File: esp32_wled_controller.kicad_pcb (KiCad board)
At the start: 4 copper layers, 95 x 95 mm, 83 parts, among them J1 USB_C_Receptacle_USB2.0_16P, J2 Screw_Terminal_01x03, J3 Screw_Terminal_01x03, J4 Screw_Terminal_01x03, J5 Screw_Terminal_01x03, J6 Screw_Terminal_01x02, J7 Screw_Terminal_01x02, K1 SRD-05VDC-SL-C, K2 SRD-05VDC-SL-C, K3 SRD-05VDC-SL-C, K4 SRD-05VDC-SL-C, Q1 Q_NPN_BEC, Q2 Q_NPN_BEC, Q3 BC547A, Q4 BC547A, Q5 BC547A, Q6 BC547A, U1 USBLC6-2P6, U2 AMS1117-3.3, U3 CP2104, U4 ESP32-SOLO1, U5 PC817, U6 PC817, U7 PC817, U8 PC817, U9 SN74AHCT125PWR

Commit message: board revision 1.1
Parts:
- removed H1, H2, H3, H4: MountingHole, MountingHole:MountingHole_2.7mm_M2.5_DIN965_Pad
- removed RX1, TX1: TestPoint, TestPoint:TestPoint_Pad_D1.0mm
- removed U4: ESP32-SOLO1, lib:ESP32SOLO1
- added H5: MountingHole_Pad, MountingHole:MountingHole_2.5mm_Pad, F.Cu at (112.1, 25.3)
- added H6: MountingHole_Pad, MountingHole:MountingHole_2.5mm_Pad, F.Cu at (25.9, 25.1)
- added H7: MountingHole_Pad, MountingHole:MountingHole_2.5mm_Pad, F.Cu at (25.4, 111.9)
- added H8: MountingHole_Pad, MountingHole:MountingHole_2.5mm_Pad, F.Cu at (112.1, 111.9)
- added RX2: TestPoint, TestPoint:TestPoint_Pad_D1.0mm, F.Cu at (88.6, 43.5)
- added TX2: TestPoint, TestPoint:TestPoint_Pad_D1.0mm, F.Cu at (85.3, 43.6)
- added U10: ESP32-S2-WROOM, lib:XCVR_ESP32-S2-WROOM, F.Cu at (107.0, 46.3)
- Q1, Q2: value Q_NPN_BEC -> SS8050
- moved 3.3V1 24.6 mm to (78.6, 43.5)
- moved GND1 23.5 mm to (81.9, 43.5)
- moved Q5 13.0 mm to (79.9, 69.0)
- moved R23 13.0 mm to (92.3, 96.1)
- moved RELAY3 13.0 mm to (75.9, 64.8)
- moved Q3 13.0 mm to (35.6, 68.8)
- moved C10 13.0 mm to (64.8, 39.3)
- moved C11 13.0 mm to (65.5, 37.4)
- moved C2 13.0 mm to (102.4, 32.5)
- moved C4 13.0 mm to (66.5, 55.5)
- moved C9 13.0 mm to (66.1, 46.1)
- moved R1 13.0 mm to (79.2, 33.3)
- moved R10 13.0 mm to (75.4, 36.3)
- moved R11 13.0 mm to (75.4, 37.5)
- moved R13 13.0 mm to (56.9, 59.5)
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- renumbered SW-BOOT1 to BOOT, SW-RESET1 to RESET
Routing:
- net /IO0: track 66.4 -> 44.5 mm
- net /STRIP4: track 47.6 -> 26.9 mm
- net /STRIP3: track 41.2 -> 24.3 mm
- net /EN: track 49.5 -> 65.3 mm
- net /IO17_RELAYS: track 93.5 -> 109.2 mm
- net /STRIP2: track 39.4 -> 26.8 mm
- net /STRIP1: track 40.3 -> 29.4 mm
- net /RX: track 47.5 -> 53.9 mm
- net GND: track 273.8 -> 270.2 mm, vias 6 -> 7
- net +3.3V: track 123.5 -> 120.9 mm
- net /TX: track 48.1 -> 45.8 mm
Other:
- board text removed: "ESP32"

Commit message: board rev 1.2, cleanup
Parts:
- removed 3.3V1, RX2, TX2: TestPoint, TestPoint:TestPoint_Pad_D1.0mm
- removed BOOT, RESET: SW_SPST, lib:TS-1187A-B-A-B
- removed C14: 100nF, Capacitor_SMD:C_0402_1005Metric_Pad0.74x0.62mm_HandSolder
- removed D5, D6, D7: 1N4007, Diode_SMD:D_MELF_Handsoldering
- removed H5: MountingHole_Pad, MountingHole:MountingHole_2.5mm_Pad
- removed R12: 1K, Resistor_SMD:R_0402_1005Metric_Pad0.72x0.64mm_HandSolder
- removed U10: ESP32-S2-WROOM, lib:XCVR_ESP32-S2-WROOM
- added 3V3: TestPoint, TestPoint:TestPoint_Pad_D1.5mm, F.Cu at (84.2, 30.3)
- added D1: C7420350, Diode_SMD:D_MELF_Handsoldering, F.Cu at (82.7, 73.2)
- added D2: C7420350, Diode_SMD:D_MELF_Handsoldering, F.Cu at (60.4, 73.1)
- added D3: C7420350, Diode_SMD:D_MELF_Handsoldering, F.Cu at (38.3, 73.1)
- added RE1: SolderJumper_2_Bridged, Jumper:SolderJumper-2_P1.3mm_Open_TrianglePad1.0x1.5mm, F.Cu at (77.5, 50.4)
- added RE2: SolderJumper_2_Bridged, Jumper:SolderJumper-2_P1.3mm_Open_TrianglePad1.0x1.5mm, F.Cu at (82.0, 50.4)
- added RE3: SolderJumper_2_Bridged, Jumper:SolderJumper-2_P1.3mm_Open_TrianglePad1.0x1.5mm, F.Cu at (86.4, 50.4)
- added REF**: OSHW-Logo_11.4x12mm_SilkScreen, Symbol:OSHW-Logo_11.4x12mm_SilkScreen, B.Cu at (108.1, 34.4)
- added RX1: TestPoint, TestPoint:TestPoint_Pad_D1.5mm, F.Cu at (114.1, 44.0)
- added SW-BOOT1: SW_SPST, lib:TS-1187A-B-A-B, F.Cu at (85.9, 36.7)
- added SW-RESET1: SW_SPST, lib:TS-1187A-B-A-B, F.Cu at (85.9, 43.5)
- added TX1: TestPoint, TestPoint:TestPoint_Pad_D1.5mm, F.Cu at (114.0, 39.5)
- added U4: EL817, Package_DIP:DIP-4_W7.62mm, F.Cu at (79.4, 61.4)
- D9: value 1N4007 -> C7420350
- GND1: footprint TestPoint:TestPoint_Pad_D1.0mm -> TestPoint:TestPoint_Pad_D1.5mm
- Q3, Q4, Q5, Q6: value BC547A -> SS8050; footprint Package_TO_SOT_SMD:TSOT-23_HandSoldering -> Package_TO_SOT_SMD:SOT-23
- U5, U6, U7: value PC817 -> EL817; footprint Package_DIP:SMDIP-4_W7.62mm -> Package_DIP:DIP-4_W7.62mm
- U8: value PC817 -> ESP32-S2-WROOM-1-N4(4MB); footprint Package_DIP:SMDIP-4_W7.62mm -> lib:WIFI-SMD_ESP32-S2-WROVER-I
- moved U5 63.6 mm to (101.7, 61.3)
- moved U7 47.7 mm to (35.0, 61.4)
- moved C13 36.4 mm to (79.1, 42.4), turned to -90 degrees
- moved C12 34.6 mm to (78.6, 46.7)
- moved U9 26.2 mm to (69.0, 84.5)
- moved U8 23.8 mm to (101.7, 40.2)
- moved C4 23.4 mm to (67.7, 78.9)
- moved R7 15.7 mm to (90.5, 35.2), turned to 90 degrees
- moved R14 15.5 mm to (74.0, 73.9)
- moved R8 15.4 mm to (29.6, 73.8)
- moved R13 15.2 mm to (51.7, 73.8)
- moved R18 15.1 mm to (96.3, 73.8)
- moved GND1 14.5 mm to (87.9, 30.3), turned to 0 degrees
- moved C2 13.2 mm to (90.5, 38.2), turned to -90 degrees
- moved C1 13.1 mm to (90.5, 45.0), turned to 90 degrees
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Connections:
- C12 pad 1: /EN -> +3.3V
- C4 pad 1: Net-(U9-GND) -> GND
- C4 pad 2: Net-(U9-VCC) -> +5V
- K1 pad A2: Net-(D5-A) -> Net-(D3-A)
- K2 pad A2: Net-(D6-A) -> Net-(D2-A)
- K3 pad A2: Net-(D7-A) -> Net-(D1-A)
- Q3 pad 1: Net-(D5-A) -> Net-(Q3-B)
- Q3 pad 2: Net-(Q3-B) -> GND
- Q3 pad 3: GND -> Net-(D3-A)
- Q4 pad 1: Net-(D6-A) -> Net-(Q4-B)
- Q4 pad 2: Net-(Q4-B) -> GND
- Q4 pad 3: GND -> Net-(D2-A)
- Q5 pad 1: Net-(D7-A) -> Net-(Q5-B)
- Q5 pad 2: Net-(Q5-B) -> GND
- Q5 pad 3: GND -> Net-(D1-A)
- Q6 pad 1: Net-(D9-A) -> Net-(Q6-B)
- Q6 pad 2: Net-(Q6-B) -> GND
- Q6 pad 3: GND -> Net-(D9-A)
- RELAY1 pad 1: /IO17_RELAYS -> /RELAY1
- RELAY2 pad 1: /IO17_RELAYS -> /RELAY2
- RELAY3 pad 1: /IO17_RELAYS -> /RELAY3
- RELAY4 pad 1: /IO17_RELAYS -> /RELAY4
- U5 pad 1: Net-(R8-Pad1) -> Net-(R18-Pad1)
- U5 pad 2: Net-(RELAY1-A) -> Net-(RELAY4-A)
- U5 pad 3: Net-(R15-Pad1) -> Net-(R19-Pad1)
- U7 pad 1: Net-(R14-Pad1) -> Net-(R8-Pad1)
- U7 pad 2: Net-(RELAY3-A) -> Net-(RELAY1-A)
- U7 pad 3: Net-(R17-Pad1) -> Net-(R15-Pad1)
- U8 pad 1: Net-(R18-Pad1) -> GND
- U8 pad 2: Net-(RELAY4-A) -> +3.3V
- U8 pad 3: Net-(R19-Pad1) -> /IO0
- U8 pad 4: +5V -> unconnected-(U8-IO1-Pad4)
- U9 pad 1: Net-(U9-GND) -> GND
- U9 pad 10: Net-(U9-GND) -> GND
- U9 pad 13: Net-(U9-GND) -> GND
- U9 pad 14: Net-(U9-VCC) -> +5V
- U9 pad 4: Net-(U9-GND) -> GND
- U9 pad 7: Net-(U9-GND) -> GND
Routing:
- net GND: track 270.2 -> 114.3 mm, vias 7 -> 9
- net /IO17_RELAYS: track 109.2 -> 0.00 mm, vias 6 -> 0
- net /RELAY1: track 0.00 -> 78.0 mm, vias 0 -> 3
- net /RELAY2: track 0.00 -> 65.1 mm, vias 0 -> 3
- net /RELAY4: track 0.00 -> 54.4 mm, vias 0 -> 3
- net /STRIP2: track 26.8 -> 70.9 mm, vias 0 -> 2
- net /RELAY3: track 0.00 -> 41.0 mm, vias 0 -> 3
- net +3.3V: track 120.9 -> 81.5 mm, vias 5 -> 6
- net /STRIP1: track 29.4 -> 66.2 mm, vias 0 -> 2
- net +5V: track 188.6 -> 153.1 mm
- net /STRIP3: track 24.3 -> 59.0 mm
- net /STRIP4: track 26.9 -> 57.6 mm
- net Net-(U9-3Y): track 53.1 -> 25.5 mm
- net Net-(U9-4Y): track 57.0 -> 29.9 mm, vias 2 -> 0
- net Net-(U9-GND): track 26.4 -> 0.00 mm, vias 3 -> 0
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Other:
- board text added: "GND 5V"
- board text added: "KEEP-OUT ZONE"
- board text added: "PWR"
- board text added: "website: jack0217.dev github: @fellettigiacomo license: CERN-OHL-S"
- board text removed: "+5V GND"
- board text removed: "3.3V PWR"
- board text removed: "USB-C"

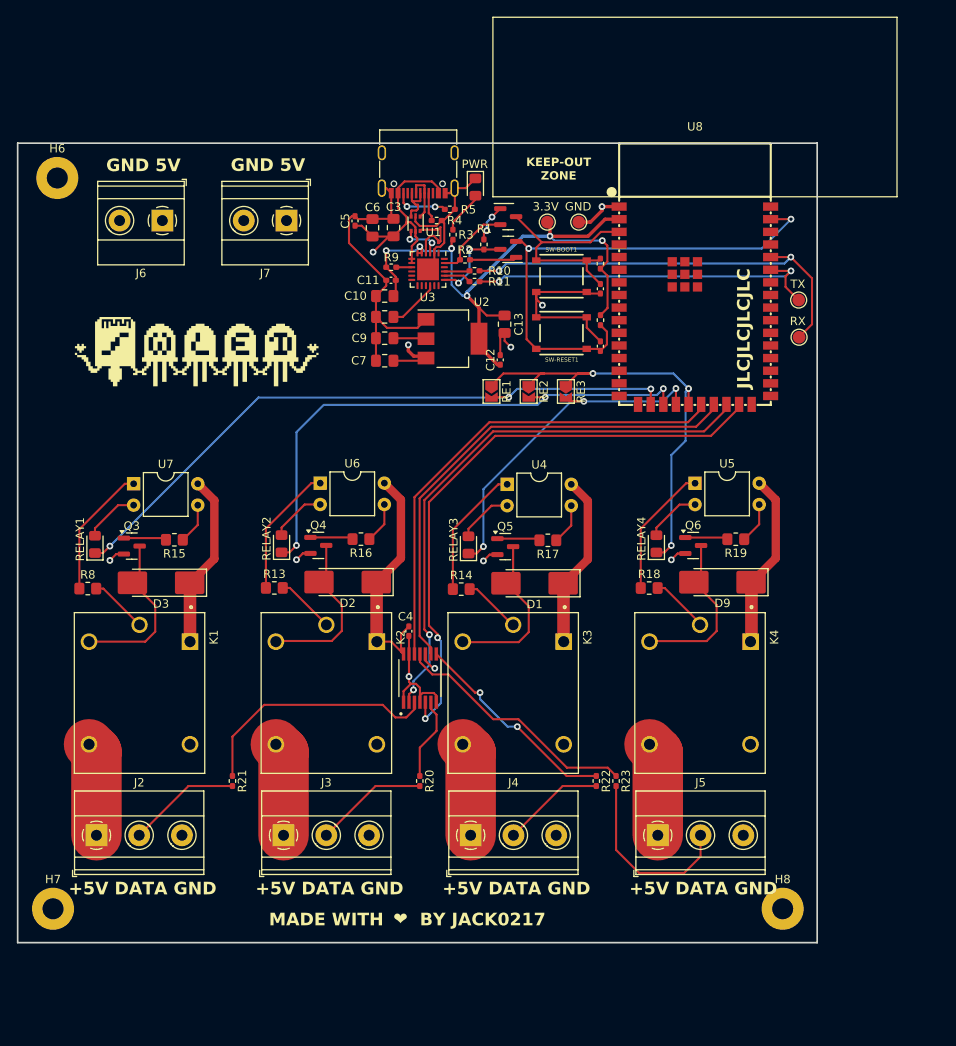
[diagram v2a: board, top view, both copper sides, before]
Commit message: changed terminal block footprint
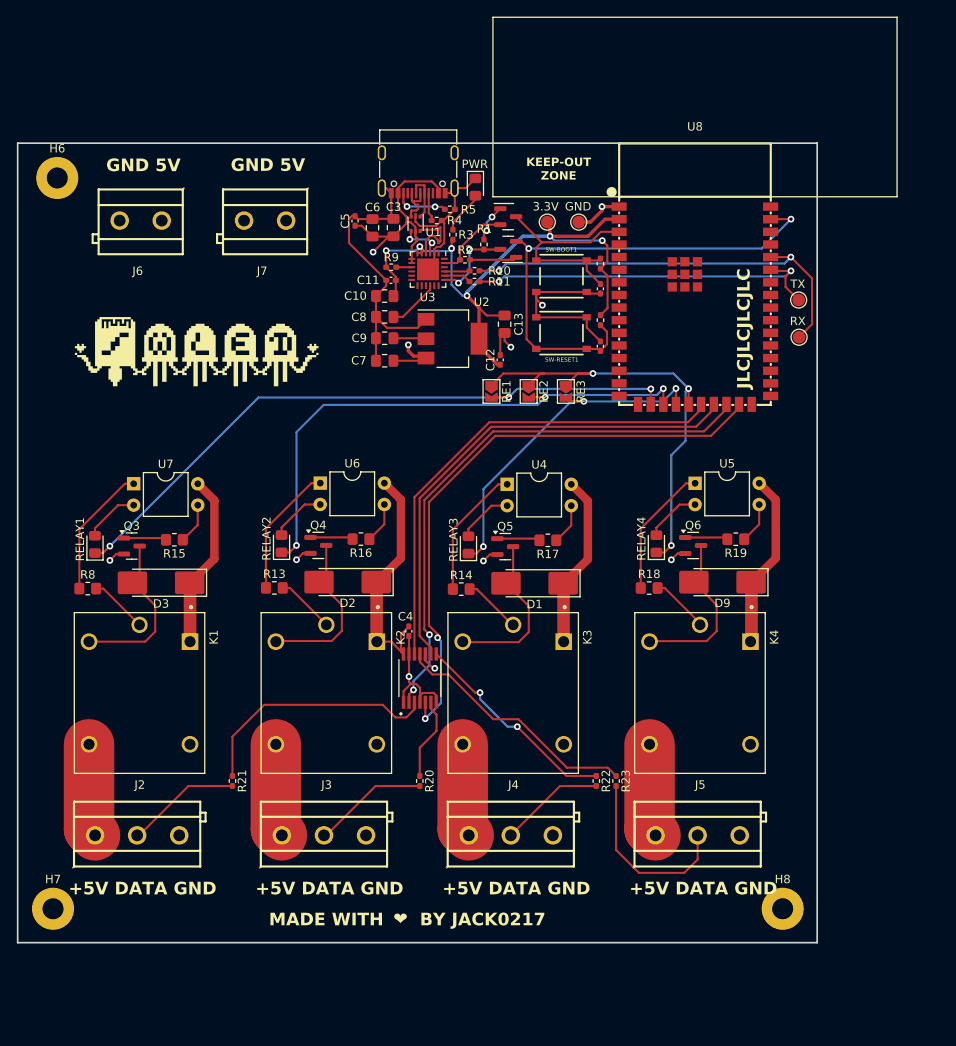
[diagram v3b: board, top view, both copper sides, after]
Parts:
- J2, J3, J4, J5: footprint TerminalBlock_Phoenix:TerminalBlock_Phoenix_MKDS-1,5-3-5.08_1x03_P5.08mm_Horizontal -> lib:CONN-TH_3P-P5.00_KF301-5.0-3P
- J6, J7: footprint TerminalBlock_Phoenix:TerminalBlock_Phoenix_MKDS-1,5-2-5.08_1x02_P5.08mm_Horizontal -> lib:CONN-TH_P5.00_KF301-5.0-2P
- moved J2 4.84 mm to (35.4, 103.2)
- moved J3 4.80 mm to (57.6, 103.2)
- moved J4 4.77 mm to (79.8, 103.2)
- moved J5 4.74 mm to (102.0, 103.2)
- moved J6 2.57 mm to (35.9, 30.1)
- moved J7 2.55 mm to (50.6, 30.1)

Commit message: final 1.2 release
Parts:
- removed SW-BOOT1, SW-RESET1: SW_SPST, lib:TS-1187A-B-A-B
- removed U1: USBLC6-2P6, Package_TO_SOT_SMD:SOT-666
- added SW1: SW_SPST, Button_Switch_SMD:SW_Push_1P1T_XKB_TS-1187A, F.Cu at (85.9, 43.4)
- added SW2: SW_SPST, Button_Switch_SMD:SW_Push_1P1T_XKB_TS-1187A, F.Cu at (85.9, 36.7)
- renumbered G*** to G***1, REF** to REF**1
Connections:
- J1 pad A6: Net-(J1-D+-PadA6) -> /D+
- J1 pad A7: Net-(J1-D--PadA7) -> /D-
- J1 pad B6: Net-(J1-D+-PadA6) -> /D+
- J1 pad B7: Net-(J1-D--PadA7) -> /D-
- J1 pad S1: GND -> unconnected-(J1-SHIELD-PadS1)_2
- U3 pad 3: Net-(U3-D+) -> /D+
- U3 pad 4: Net-(U3-D-) -> /D-
- U8 pad 42: unconnected-(U8-GND-Pad42) -> GND
- U8 pad 43: unconnected-(U8-GND-Pad43)_1 -> GND
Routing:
- net /D+: track 0.00 -> 13.6 mm, vias 0 -> 2
- net /D-: track 0.00 -> 12.0 mm, vias 0 -> 2
- net Net-(U3-D-): track 8.43 -> 0.00 mm
- net +3.3V: track 81.5 -> 87.8 mm
- net Net-(J1-D+-PadA6): track 5.86 -> 0.00 mm
- net Net-(J1-D--PadA7): track 5.86 -> 0.00 mm
- net Net-(U3-D+): track 5.07 -> 0.00 mm, vias 2 -> 0
- net +5V: track 153.1 -> 151.1 mm
- net GND: track 114.3 -> 113.8 mm, vias 9 -> 16
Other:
- board text added: "BOOT"
- board text added: "RESET"

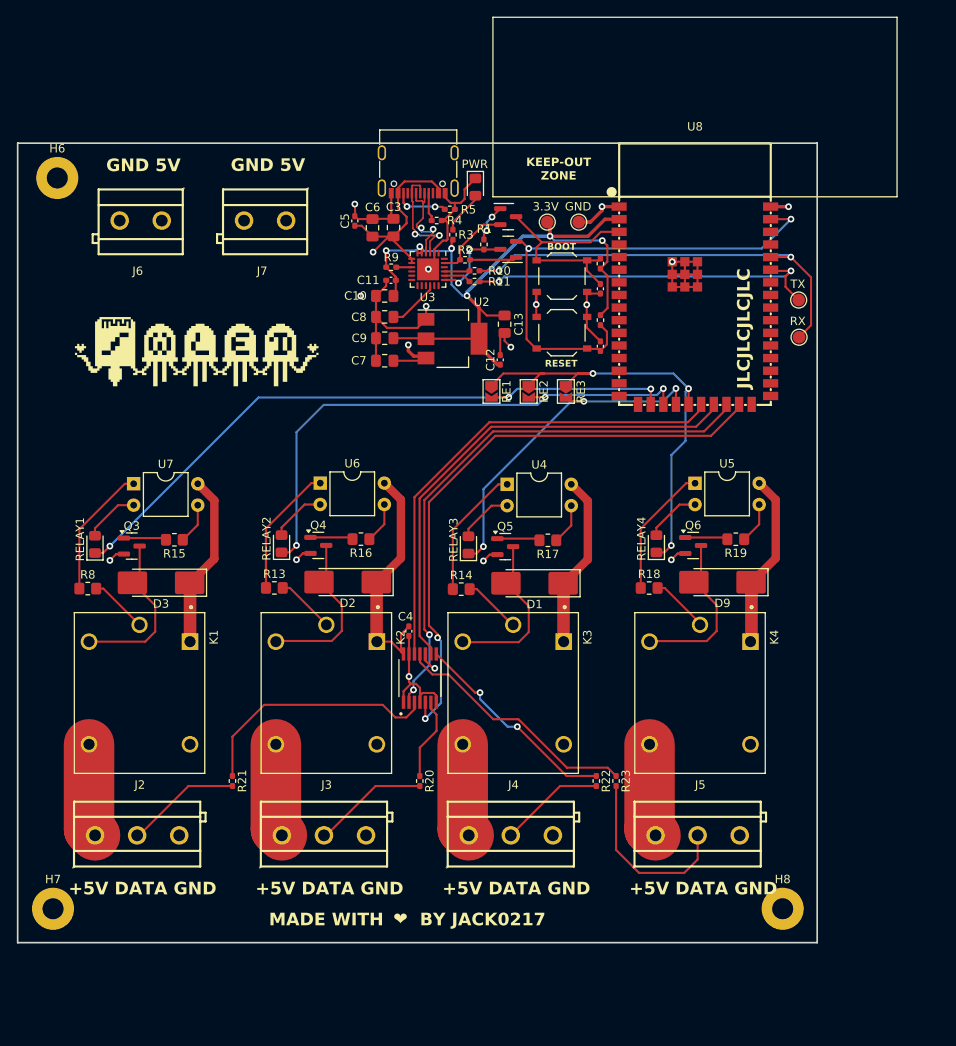
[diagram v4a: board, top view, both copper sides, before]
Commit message: fix optocoupler footprint, fix layout
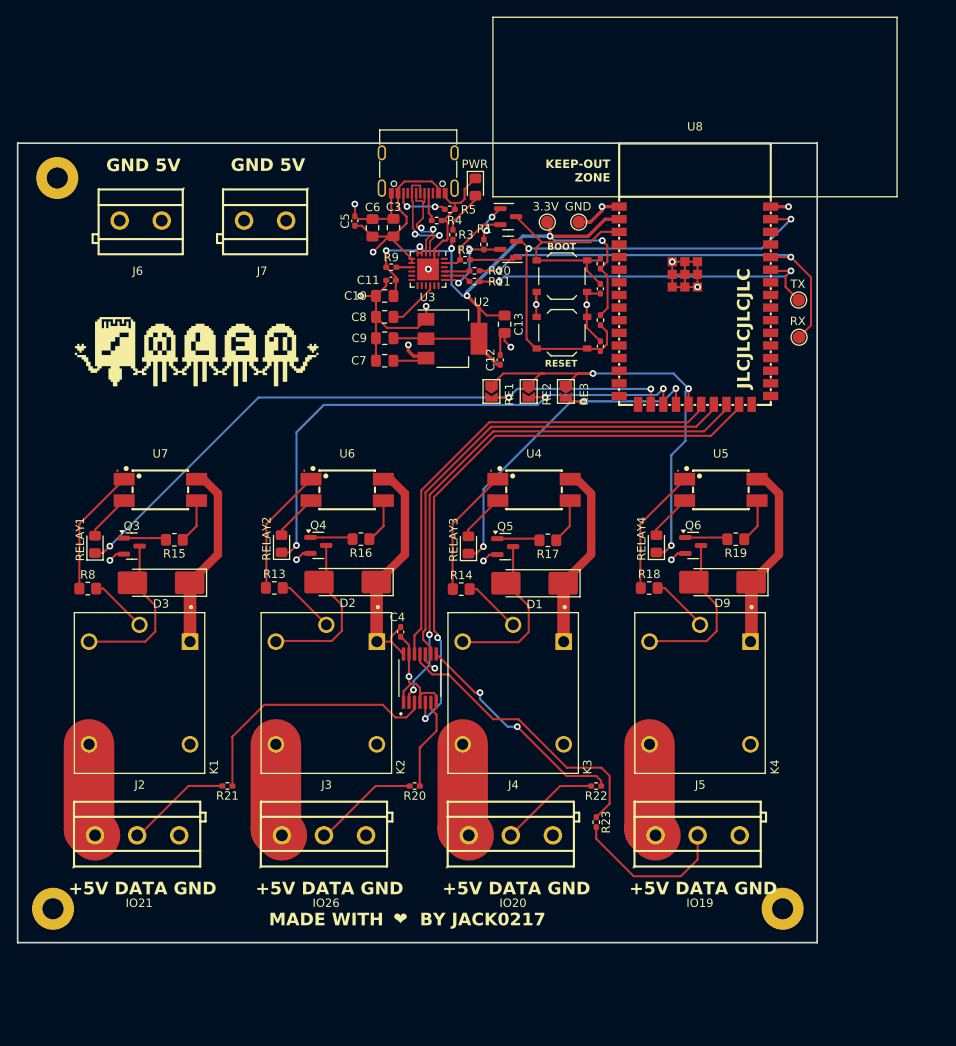
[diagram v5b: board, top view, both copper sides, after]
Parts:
- U4, U5, U6, U7: footprint Package_DIP:DIP-4_W7.62mm -> lib:OPTO-SMD-4_L4.6-W6.5-P2.54-LS10.3-TL
- moved R23 5.43 mm to (90.0, 101.6)
- moved REF**1 3.50 mm to (106.1, 37.2)
- moved U6 3.30 mm to (60.4, 62.1)
- moved U4 3.26 mm to (82.6, 62.1)
- moved U7 3.26 mm to (38.2, 62.1)
- moved U5 3.17 mm to (104.8, 62.1)
- moved C4 0.97 mm to (66.8, 79.0)
- moved R20 0.85 mm to (68.4, 97.3), turned to 180 degrees
- moved R21 0.84 mm to (46.2, 97.3), turned to 180 degrees
- moved R22 0.60 mm to (90.0, 97.3), turned to 180 degrees
- renumbered RE3 to JP1, RE2 to JP2, RE1 to JP3
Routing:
- net Net-(U9-4Y): track 29.9 -> 34.7 mm
- net /BDATA_STRIP4: track 21.9 -> 19.0 mm
- net GND: track 113.8 -> 116.0 mm, vias 16 -> 17
- net +5V: track 151.1 -> 153.1 mm
- net Net-(U9-3Y): track 25.5 -> 26.9 mm
- net Net-(U9-2Y): track 9.86 -> 11.2 mm
- net /BDATA_STRIP2: track 13.8 -> 12.6 mm
- net /BDATA_STRIP1: track 13.8 -> 12.6 mm
- net Net-(U9-1Y): track 29.7 -> 30.9 mm
- net Net-(RELAY1-A): track 6.62 -> 5.62 mm
- net Net-(RELAY4-A): track 6.62 -> 5.62 mm
- net Net-(RELAY3-A): track 6.62 -> 5.62 mm
- net Net-(RELAY2-A): track 6.62 -> 5.62 mm
- net /BDATA_STRIP3: track 12.4 -> 11.8 mm
- net Net-(R14-Pad1): track 15.7 -> 15.2 mm
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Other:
- board text added: "ESP32-WLED-4ch-controller V1.2"
- board text added: "IO19"
- board text added: "IO20"
- board text added: "IO21"
- board text added: "IO26"
- board text added: "RE1"
- board text added: "RE2"
- board text added: "RE3"
